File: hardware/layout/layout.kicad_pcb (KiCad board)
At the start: 4 copper layers, 50 x 22 mm, 74 parts, among them J1 208658-1001, J2 USB4105-GF-A-060, Q1 2N7002, SW1 TS-1088-AR02016, U1 PCA9306DCTR, U2 AP2112K-3.3TRG1, U3 USBLC6-2SC6, U4 W25Q16JVSSIQ, U5 RP2040, Y1 X322512MSB4SI

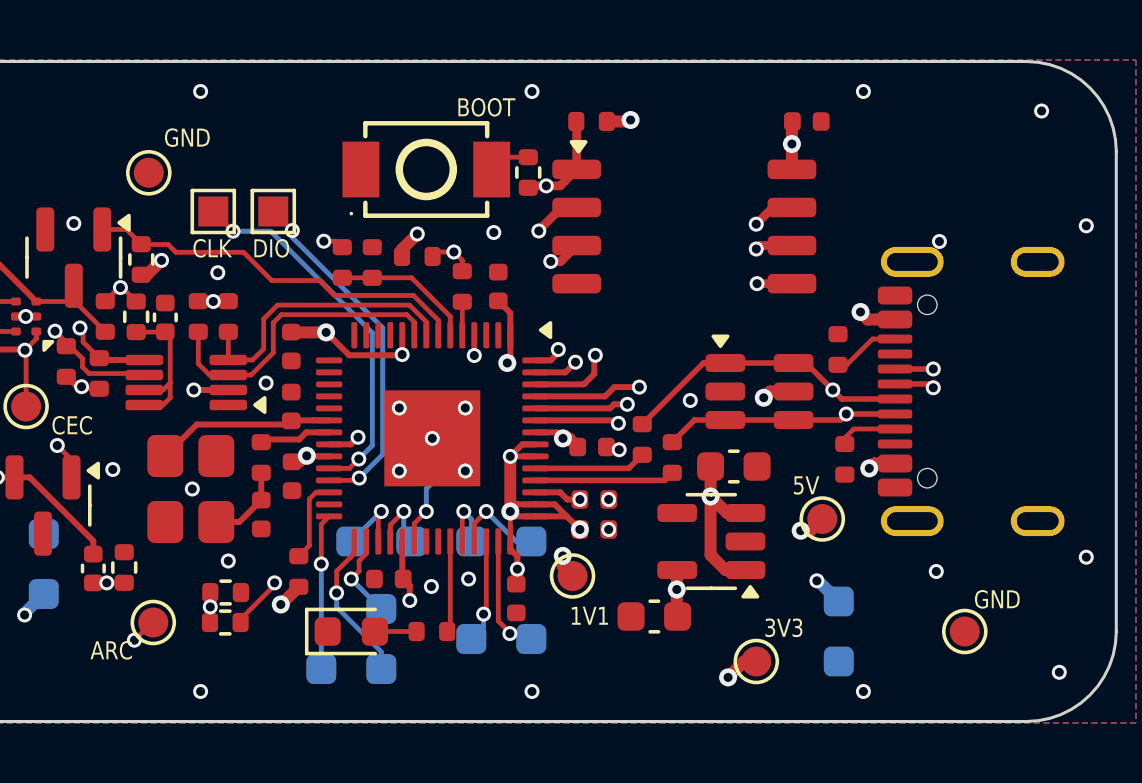
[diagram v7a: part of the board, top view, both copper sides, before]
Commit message: fix: angular USB diff pair go!
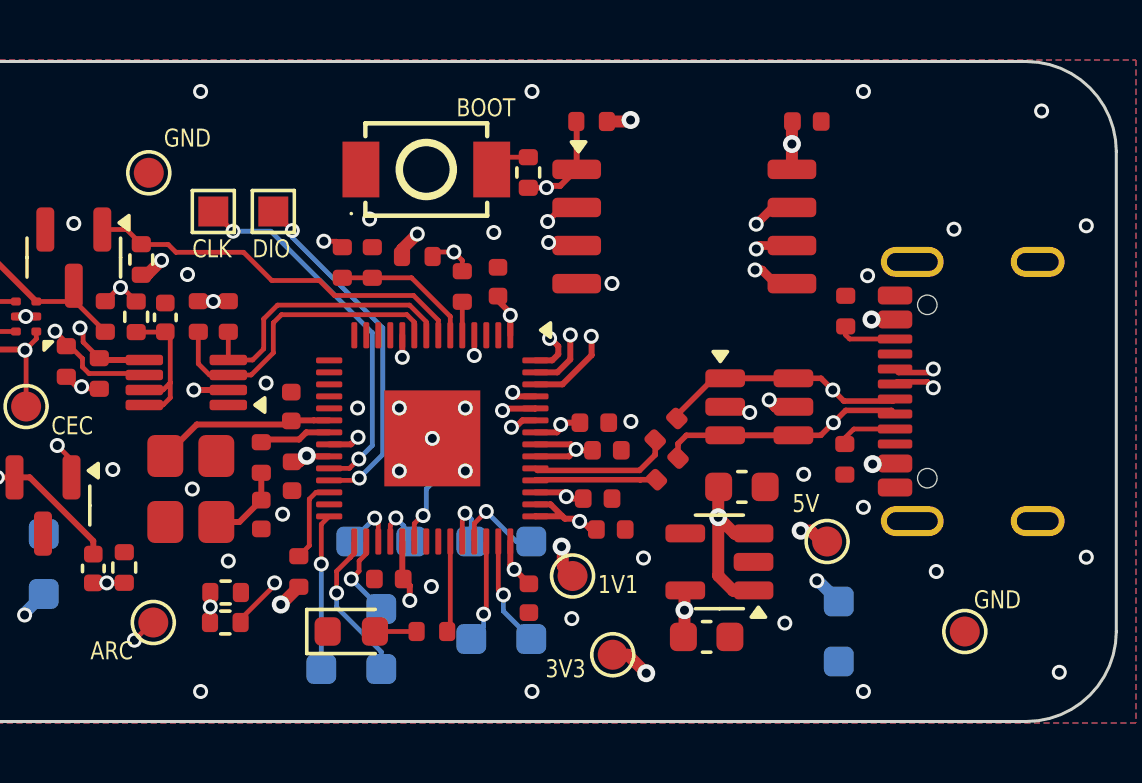
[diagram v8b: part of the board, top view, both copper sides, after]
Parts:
- moved C11 11.1 mm to (133.0, 113.0), turned to 0 degrees
- moved TP16 4.79 mm to (133.2, 119.8)
- moved C4 1.87 mm to (136.3, 119.2), turned to 0 degrees
- moved R18 1.31 mm to (141.0, 108.3)
- moved R22 0.86 mm to (135.0, 112.3), turned to 45 degrees
- moved C8 0.81 mm to (132.6, 112.0)
- moved TP17 0.77 mm to (140.4, 116.0)
- moved C3 0.73 mm to (137.5, 114.2)
- moved U2 0.73 mm to (136.8, 116.7)
- moved C10 0.55 mm to (133.2, 115.6)
- moved U3 0.51 mm to (138.1, 111.5)
- moved C13 0.42 mm to (130.4, 117.9)
- moved R21 0.42 mm to (135.0, 113.6), turned to 45 degrees
- moved C7 0.16 mm to (129.4, 107.3)
- moved C9 0.11 mm to (132.7, 114.6)
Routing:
- net VDD_3V3: track 31.7 -> 24.8 mm, vias 19 -> 17
- net QSPI_IO3: track 13.1 -> 15.6 mm
- net QSPI_CLK: track 11.6 -> 13.7 mm
- net QSPI_IO0: track 10.3 -> 12.2 mm
- net USB_D_P: track 14.7 -> 13.2 mm
- net USB_D_N: track 12.8 -> 13.9 mm
- net U_MCU.RP_USB_D_P: track 3.75 -> 4.72 mm
- net VDD_5V: track 10.9 -> 10.2 mm
- net U_MCU.RP_USB_D_N: track 4.67 -> 4.04 mm
- net VDD_1V1: track 5.32 -> 5.88 mm
- net GP20: track 2.46 -> 1.93 mm
- net GND: vias 39 -> 46
